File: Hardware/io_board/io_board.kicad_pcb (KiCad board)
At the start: 2 copper layers, 80.8 x 60.1 mm, 34 parts, among them J1 Conn_01x40, J2 Conn_02x06_Odd_Even, J3 Mini-DIN-6, J4 Conn_02x10_Odd_Even, U1 74LS138, U2 W65C22NxP, U3 74LS14

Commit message: Fix LED orientation + move resistor under socket
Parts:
- moved R4 11.4 mm to (59.4, -19.1), turned to 90 degrees
- moved D3 2.54 mm to (33.0, -50.5)
- moved D4 2.54 mm to (27.9, -50.5)
- moved D6 2.54 mm to (12.7, -50.5)
- moved D1 2.54 mm to (43.2, -50.5)
- moved D2 2.54 mm to (33.0, -50.5)
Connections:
- D1 pad 1: /PA0 -> Net-(D1-Pad1)
- D1 pad 2: Net-(D1-Pad2) -> /PA0
- D2 pad 1: /PA1 -> Net-(D2-Pad1)
- D2 pad 2: Net-(D2-Pad2) -> /PA1
- D3 pad 1: /PA2 -> Net-(D3-Pad1)
- D3 pad 2: Net-(D3-Pad2) -> /PA2
- D4 pad 1: /PA3 -> Net-(D4-Pad1)
- D4 pad 2: Net-(D4-Pad2) -> /PA3
- D5 pad 1: /PA4 -> Net-(D5-Pad1)
- D5 pad 2: Net-(D5-Pad2) -> /PA4
- D6 pad 1: /PA5 -> Net-(D6-Pad1)
- D6 pad 2: Net-(D6-Pad2) -> /PA5
- D7 pad 1: /PA6 -> Net-(D7-Pad1)
- D7 pad 2: Net-(D7-Pad2) -> /PA6
- D8 pad 1: /PA7 -> Net-(D8-Pad1)
- D8 pad 2: Net-(D8-Pad2) -> /PA7
- R10 pad 1: Net-(D6-Pad2) -> Net-(D6-Pad1)
- R11 pad 1: Net-(D7-Pad2) -> Net-(D7-Pad1)
- R12 pad 1: Net-(D8-Pad2) -> Net-(D8-Pad1)
- R5 pad 1: Net-(D1-Pad2) -> Net-(D1-Pad1)
- R6 pad 1: Net-(D2-Pad2) -> Net-(D2-Pad1)
- R7 pad 1: Net-(D3-Pad2) -> Net-(D3-Pad1)
- R8 pad 1: Net-(D4-Pad2) -> Net-(D4-Pad1)
- R9 pad 1: Net-(D5-Pad2) -> Net-(D5-Pad1)
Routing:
- net Net-(D8-Pad2): track 9.60 -> 0.00 mm
- net Net-(D8-Pad1): track 0.00 -> 9.60 mm
- net Net-(D2-Pad2): track 9.24 -> 0.00 mm
- net Net-(D2-Pad1): track 0.00 -> 9.24 mm
- net Net-(D1-Pad2): track 8.65 -> 0.00 mm
- net Net-(D1-Pad1): track 0.00 -> 8.65 mm
- net Net-(D7-Pad2): track 7.12 -> 0.00 mm
- net Net-(D7-Pad1): track 0.00 -> 7.12 mm
- net Net-(D3-Pad2): track 5.84 -> 0.00 mm
- net Net-(D3-Pad1): track 0.00 -> 5.84 mm
- net Net-(D6-Pad2): track 5.69 -> 0.00 mm
- net Net-(D6-Pad1): track 0.00 -> 5.69 mm
- net Net-(D5-Pad2): track 4.84 -> 0.00 mm
- net Net-(D5-Pad1): track 0.00 -> 4.84 mm
- net Net-(D4-Pad2): track 4.63 -> 0.00 mm
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
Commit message: update IO board gerbers
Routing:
- net ~SLOT_SEL~: track 77.1 -> 79.3 mm
- net D0: track 52.9 -> 54.8 mm
- net A0: track 38.8 -> 38.2 mm

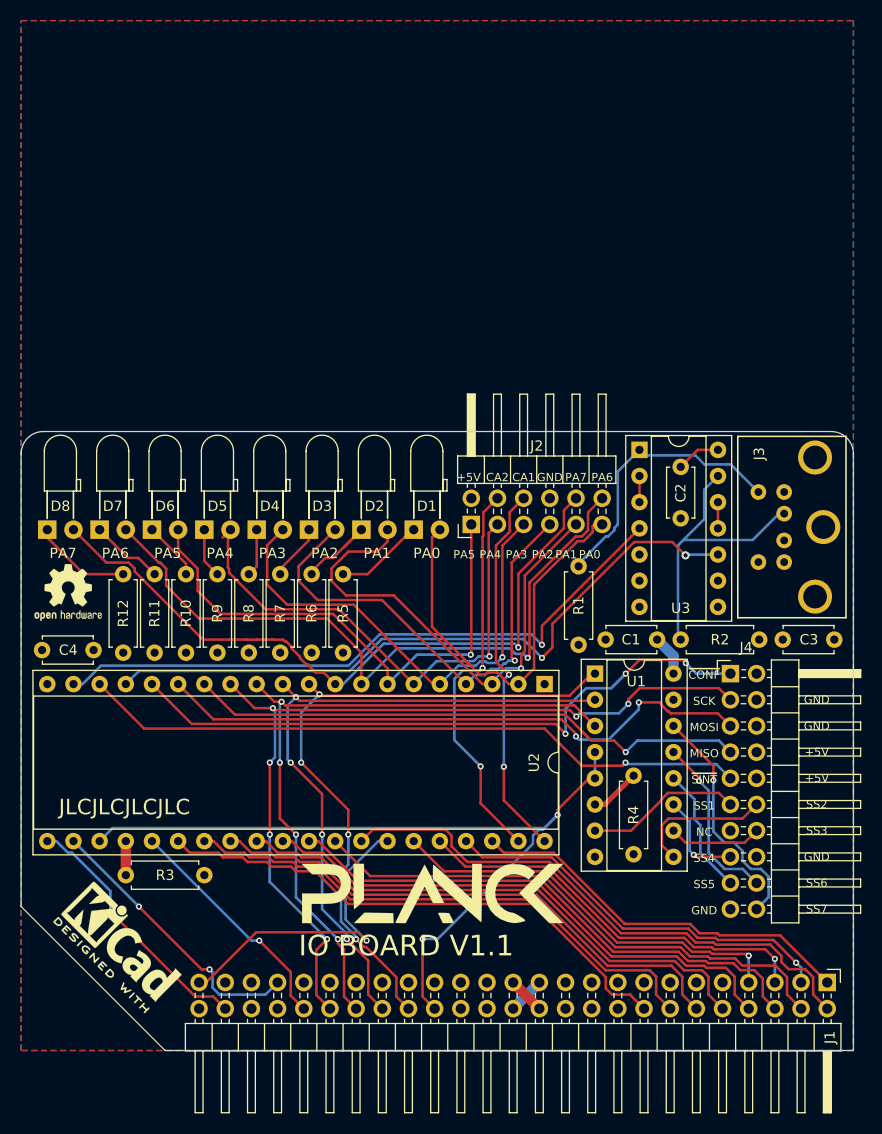
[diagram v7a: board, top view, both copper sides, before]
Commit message: Add internal PS2 header
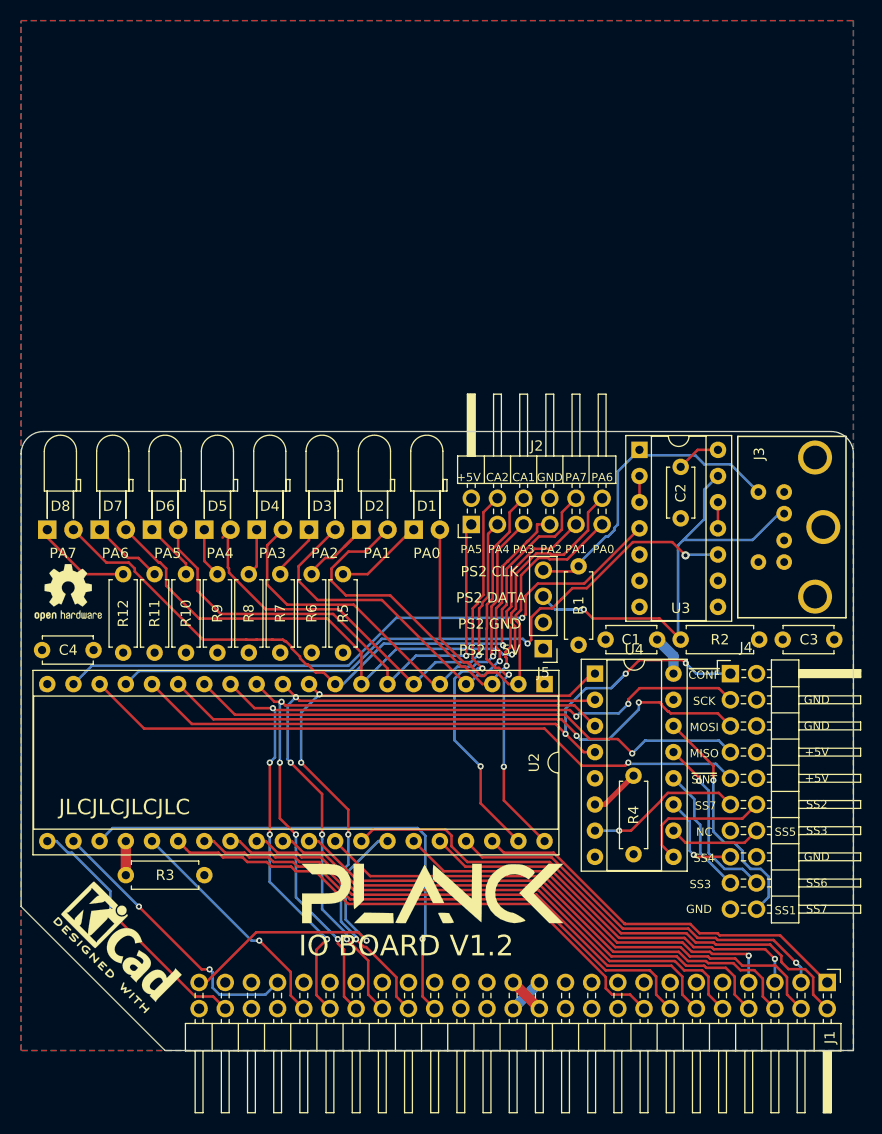
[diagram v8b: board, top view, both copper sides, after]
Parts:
- removed U1: 74LS138, Package_DIP:DIP-16_W7.62mm_Socket
- added J5: Conn_01x04_Male, Connector_PinHeader_2.54mm:PinHeader_1x04_P2.54mm_Vertical, F.Cu at (50.7, -39.0)
- added U4: 74HC137, Package_DIP:DIP-16_W7.62mm_Socket, F.Cu at (55.7, -36.6)
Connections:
- net R~W~ renamed R~{W}
- net ~CONF~ renamed ~{CONF}
- net ~INH~ renamed ~{INH}
- net ~IRQ~ renamed ~{IRQ}
- net ~NMI~ renamed ~{NMI}
- net ~RESET~ renamed ~{RESET}
- net ~SINT~ renamed ~{SINT}
- net ~SLOT_IRQ~ renamed ~{SLOT_IRQ}
- net ~SLOT_SEL~ renamed ~{SLOT_SEL}
- net ~SLOW~ renamed ~{SLOW}
- net ~SSEL~ renamed ~{SSEL}
- J3 pad 2: Net-(J3-Pad2) -> unconnected-(J3-Pad2)
- J3 pad 6: Net-(J3-Pad6) -> unconnected-(J3-Pad6)
- J4 pad 11: /SS1 -> /SS7
- J4 pad 12: /SS2 -> /SS6
- J4 pad 13: Net-(J4-Pad13) -> unconnected-(J4-Pad13)
- J4 pad 14: /SS3 -> /SS5
- J4 pad 17: /SS5 -> /SS3
- J4 pad 18: /SS6 -> /SS2
- J4 pad 20: /SS7 -> /SS1
- U3 pad 6: Net-(U3-Pad6) -> unconnected-(U3-Pad6)
- U3 pad 8: Net-(U3-Pad8) -> unconnected-(U3-Pad8)
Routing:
- net ~{SLOT_SEL}: track 79.3 -> 49.8 mm, vias 2 -> 1
- net PS2_DATA: track 28.2 -> 43.2 mm, vias 0 -> 1
- net /SS1: track 15.2 -> 23.2 mm, vias 0 -> 1
- net /SS7: track 23.2 -> 15.2 mm
- net /SS5: track 13.0 -> 9.04 mm
- net /SS3: track 9.04 -> 13.0 mm
- net Net-(J3-Pad5): track 27.2 -> 30.9 mm
- net ~{CONF}: track 64.9 -> 68.5 mm
- net /SS6: track 17.1 -> 13.6 mm, vias 1 -> 0
- net /SS2: track 13.6 -> 17.1 mm, vias 0 -> 1
- net /PA0: track 41.4 -> 43.2 mm
- net Net-(U2-Pad17): track 66.6 -> 65.4 mm
- net /CA1: track 36.8 -> 37.9 mm
- net MISO: track 55.7 -> 54.8 mm
- net Net-(U2-Pad19): track 63.1 -> 62.3 mm
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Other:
- net class Default removed
- board text added: "IO BOARD V1.2"
- board text added: "PS2 +5V"
- board text added: "PS2 CLK"
- board text added: "PS2 DATA"
- board text added: "PS2 GND"
- board text added: "~{CONF}"
- board text added: "~{SINT}"
- board text removed: "~CONF~"
- board text removed: "~SINT~"
